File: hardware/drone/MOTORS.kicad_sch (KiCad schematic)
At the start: 0 parts

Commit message: save before axing motor driver ic's
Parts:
- added C17, C22: 2u2, MBASx168, symbol Device:C
- added C18, C20: 10u, SamacSys_Parts:CAPC1608X80N, symbol Device:C
- added C19, C21: 10n, CAPC2012X90N, symbol Device:C
- added IC2, IC3: DRV8833RTYR, QFN65P400X400X80-17N-D, symbol SamacSys_Parts:DRV8833RTYR
- added TP10: A2, SamacSys_Parts:Motor solder point, symbol Connector:TestPoint_Alt
- added TP11: B1, SamacSys_Parts:Motor solder point, symbol Connector:TestPoint_Alt
- added TP12: B2, SamacSys_Parts:Motor solder point, symbol Connector:TestPoint_Alt
- added TP13: C1, SamacSys_Parts:Motor solder point, symbol Connector:TestPoint_Alt
- added TP14: D1, SamacSys_Parts:Motor solder point, symbol Connector:TestPoint_Alt
- added TP15: C2, SamacSys_Parts:Motor solder point, symbol Connector:TestPoint_Alt
- added TP16: D2, SamacSys_Parts:Motor solder point, symbol Connector:TestPoint_Alt
- added TP9: A1, SamacSys_Parts:Motor solder point, symbol Connector:TestPoint_Alt
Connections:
- new net: C22.2, IC3.12 (VINT)
- new net: C21.2, IC3.9 (VCP)
- new net: C19.2, IC2.9 (VCP)
- new net: C17.2, IC2.12 (VINT)
- new net +BATT: C18.1, C19.1, C20.1, C21.1, IC2.10 (VM), IC3.10 (VM)
- new net A1: IC2.16 (AOUT1), TP9.1
- new net A2: IC2.2 (AOUT2), TP10.1
- new net B1: IC2.5 (BOUT1), TP11.1
- new net B2: IC2.3 (BOUT2), TP12.1
- new net C1: IC3.16 (AOUT1), TP13.1
- new net C2: IC3.2 (AOUT2), TP15.1
- new net D1: IC3.5 (BOUT1), TP14.1
- new net D2: IC3.3 (BOUT2), TP16.1
- new net GND: C17.1, C18.2, C20.2, C22.1, IC2.1 (AISEN), IC2.11 (GND_1), IC2.17 (GND_2), IC2.4 (BISEN), IC3.1 (AISEN), IC3.11 (GND_1), IC3.17 (GND_2), IC3.4 (BISEN)
- new net MD.AIN1: IC2.14 (AIN1)
- new net MD.AIN2: IC2.13 (AIN2)
- new net MD.BIN1: IC2.7 (BIN1)
- new net MD.BIN2: IC2.8 (BIN2)
- new net MD.CIN1: IC3.14 (AIN1)
- new net MD.CIN2: IC3.13 (AIN2)
- new net MD.DIN1: IC3.7 (BIN1)
- new net MD.DIN2: IC3.8 (BIN2)
- new net NFAULT1: IC2.6 (NFAULT)
- new net NFAULT2: IC3.6 (NFAULT)
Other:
- note added: "Hierarchical Labels"
- note added: "Motor Drivers"
- note added: "Motors A & B"
- note added: "Motors C & D"
- note added: "Note: motor leads will be soldered directly to driver outputs"

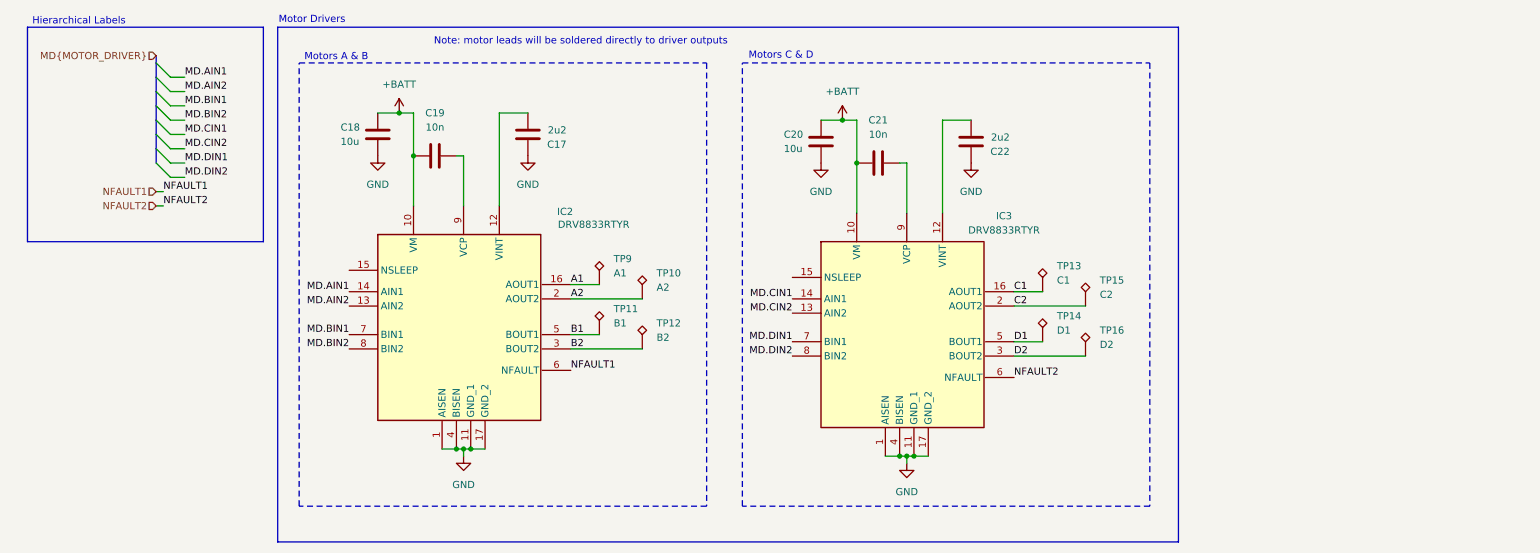
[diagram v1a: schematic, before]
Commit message: axed motor drivers. finished layout for drone but need to review overall system design after reading some stuff
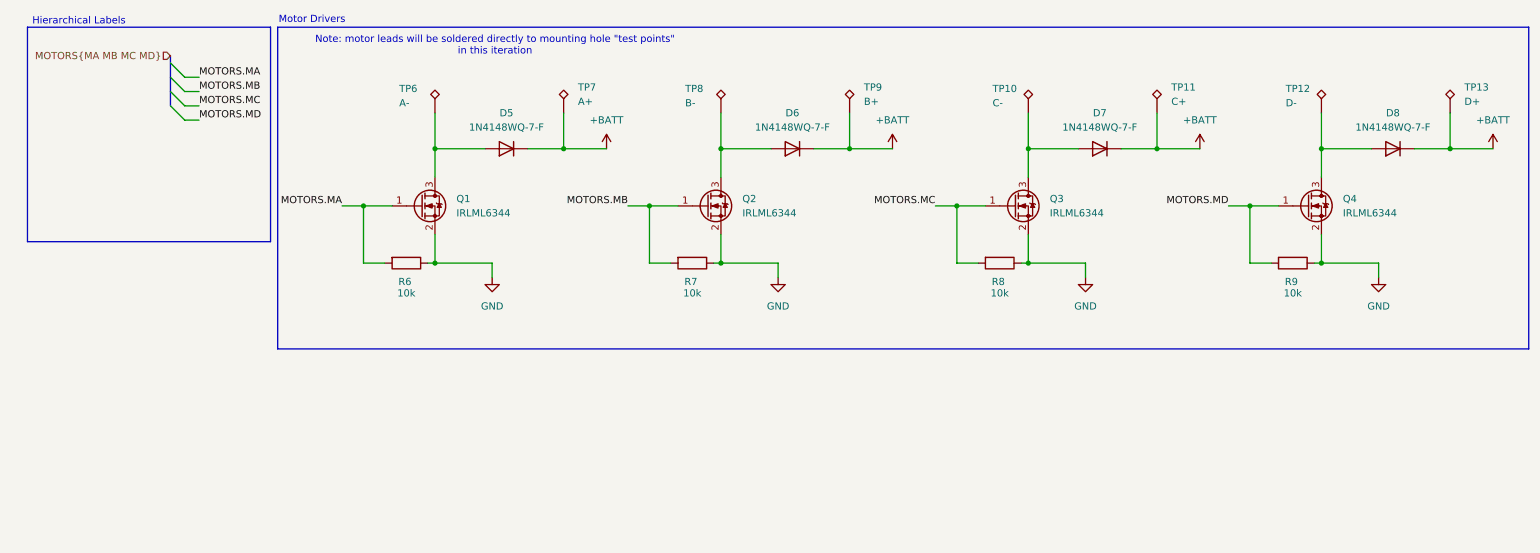
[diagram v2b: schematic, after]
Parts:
- removed C17, C22: 2u2, MBASx168, symbol Device:C
- removed C18, C20: 10u, SamacSys_Parts:CAPC1608X80N, symbol Device:C
- removed C19, C21: 10n, CAPC2012X90N, symbol Device:C
- removed IC2, IC3: DRV8833RTYR, QFN65P400X400X80-17N-D, symbol SamacSys_Parts:DRV8833RTYR
- removed TP14: D1, SamacSys_Parts:Motor solder point, symbol Connector:TestPoint_Alt
- removed TP15: C2, SamacSys_Parts:Motor solder point, symbol Connector:TestPoint_Alt
- removed TP16: D2, SamacSys_Parts:Motor solder point, symbol Connector:TestPoint_Alt
- added D5, D6, D7, D8: 1N4148WQ-7-F, SamacSys_Parts:SOD3716X145N, symbol Device:D
- added Q1, Q2, Q3, Q4: IRLML6344, Package_TO_SOT_SMD:SOT-23, symbol Transistor_FET:IRLML6244
- added R6, R7, R8, R9: 10k, SamacSys_Parts:RESC2012X60N, symbol Device:R
- added TP6: A-, SamacSys_Parts:Motor solder point, symbol Connector:TestPoint_Alt
- added TP7: A+, SamacSys_Parts:Motor solder point, symbol Connector:TestPoint_Alt
- added TP8: B-, SamacSys_Parts:Motor solder point, symbol Connector:TestPoint_Alt
- TP10: value A2 -> C-
- TP11: value B1 -> C+
- TP12: value B2 -> D-
- TP13: value C1 -> D+
- TP9: value A1 -> B+
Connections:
- net A1 is gone; now on net +BATT: TP9.1
- net B1 is gone; now on net +BATT: TP11.1
- net C1 is gone; now on net +BATT: TP13.1
- net +BATT: now also D5.1 (K), D6.1 (K), D7.1 (K), D8.1 (K), TP7.1
- net GND: now also Q1.2 (S), Q2.2 (S), Q3.2 (S), Q4.2 (S), R6.1, R7.1, R8.1, R9.1
- net A2: no longer names the net of TP10.1
- net A2: now also D7.2 (A), Q3.3 (D)
- net B2: no longer names the net of TP12.1
- net B2: now also D8.2 (A), Q4.3 (D)
- new net: D5.2 (A), Q1.3 (D), TP6.1
- new net: D6.2 (A), Q2.3 (D), TP8.1
- new net MOTORS.MA: Q1.1 (G), R6.2
- new net MOTORS.MB: Q2.1 (G), R7.2
- new net MOTORS.MC: Q3.1 (G), R8.2
- new net MOTORS.MD: Q4.1 (G), R9.2
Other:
- note added: "Note: motor leads will be soldered directly to mounting hole "test points" in this iteration"
- note removed: "Motors A & B"
- note removed: "Motors C & D"
- note removed: "Note: motor leads will be soldered directly to driver outputs"
